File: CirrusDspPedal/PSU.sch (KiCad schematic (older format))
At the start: 5 parts, among them J4 Barrel_Jack_Switch, U5 MCP1700-3302E_SOT23

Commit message: Added Footswitches and relay
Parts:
- D1: footprint (none) -> Diode_SMD:D_SOD-123F
- J4: footprint (none) -> Connector_BarrelJack:BarrelJack_Horizontal
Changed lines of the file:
@@
 $Descr A4 11693 8268
 encoding utf-8
-Sheet 8 8
+Sheet 8 10
 Title ""
 Date ""
@@
 F 0 "D1" H 4800 3358 50  0000 C CNN
 F 1 "D_Schottky" H 4800 3449 50  0000 C CNN
-F 2 "" H 4800 3575 50  0001 C CNN
+F 2 "Diode_SMD:D_SOD-123F" H 4800 3575 50  0001 C CNN
 F 3 "~" H 4800 3575 50  0001 C CNN
 	1    4800 3575
@@
 F 0 "J4" H 2950 3375 50  0000 R CNN
 F 1 "Barrel_Jack_Switch" H 3575 3450 50  0000 R CNN
-F 2 "" H 3125 3635 50  0001 C CNN
+F 2 "Connector_BarrelJack:BarrelJack_Horizontal" H 3125 3635 50  0001 C CNN
 F 3 "~" H 3125 3635 50  0001 C CNN
 	1    3075 3675

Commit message: Completed schematic design
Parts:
- added J7: Conn_01x01, TestPoint:TestPoint_Pad_2.0x2.0mm, symbol Connector_Generic:Conn_01x01
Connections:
- new net GNDPWR: J7.1 (Pin_1)
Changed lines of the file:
@@
 $Descr A4 11693 8268
 encoding utf-8
-Sheet 8 10
+Sheet 6 11
 Title ""
 Date ""
@@
 Wire Wire Line
 	7525 3575 8700 3575
+$Comp
+L power:GNDPWR #PWR016
+U 1 1 5FB2677B
+P 5575 5950
+F 0 "#PWR016" H 5575 5750 50  0001 C CNN
+F 1 "GNDPWR" H 5579 5796 50  0000 C CNN
+F 2 "" H 5575 5900 50  0001 C CNN
+F 3 "" H 5575 5900 50  0001 C CNN
+	1    5575 5950
+	1    0    0    -1
+$EndComp
+Wire Wire Line
+	5575 5950 5575 5825
+$Comp
+L Connector_Generic:Conn_01x01 J7
+U 1 1 5FB27261
+P 5575 5525
+F 0 "J7" V 5493 5437 50  0000 R CNN
+F 1 "Conn_01x01" V 5448 5437 50  0001 R CNN
+F 2 "TestPoint:TestPoint_Pad_2.0x2.0mm" H 5575 5525 50  0001 C CNN
+F 3 "~" H 5575 5525 50  0001 C CNN
+	1    5575 5525
+	0    -1   -1   0
+$EndComp
+$Comp
+L power:PWR_FLAG #FLG0106
+U 1 1 5FB29381
+P 5775 5825
+F 0 "#FLG0106" H 5775 5900 50  0001 C CNN
+F 1 "PWR_FLAG" H 5775 5998 50  0001 C CNN
+F 2 "" H 5775 5825 50  0001 C CNN
+F 3 "~" H 5775 5825 50  0001 C CNN
+	1    5775 5825
+	0    1    1    0
+$EndComp
+Wire Wire Line
+	5775 5825 5575 5825
+Connection ~ 5575 5825
+Wire Wire Line
+	5575 5825 5575 5725
 $EndSCHEMATC

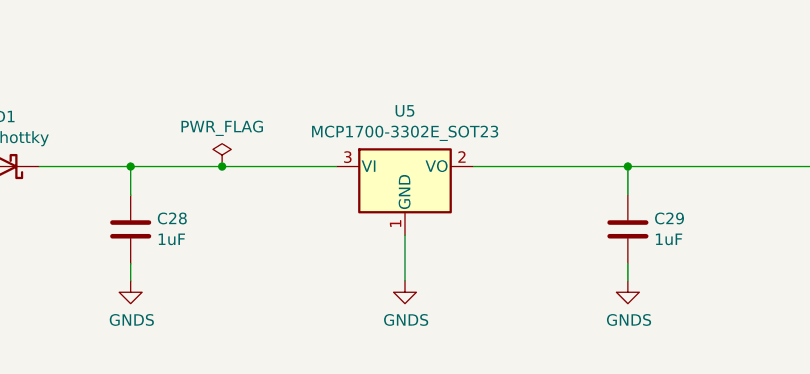
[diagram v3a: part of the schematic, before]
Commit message: updated design and layout
- Changed LDO to 1703 (footprint unchanged)
- Changed THT LEDs from RAGB (incorrect) to RCGB (correct) symbol (footprint unchanged)
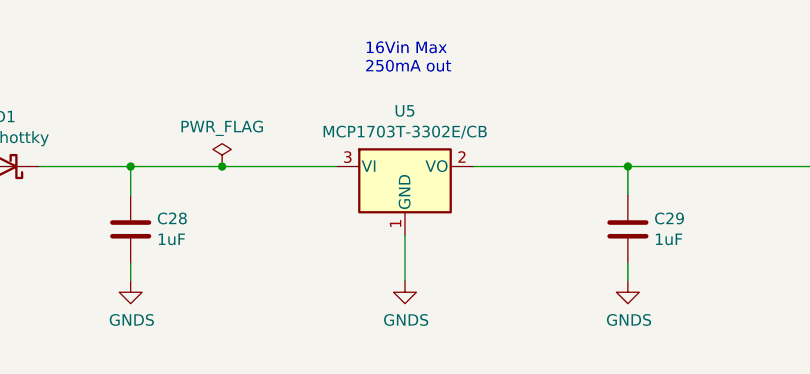
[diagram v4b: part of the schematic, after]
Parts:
- U5: value MCP1700-3302E_SOT23 -> MCP1703T-3302E/CB
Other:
- note added: "16Vin Max\n250mA out"
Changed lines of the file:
@@
 P 6550 3575
 F 0 "U5" H 6550 3817 50  0000 C CNN
-F 1 "MCP1700-3302E_SOT23" H 6550 3726 50  0000 C CNN
+F 1 "MCP1703T-3302E/CB" H 6550 3726 50  0000 C CNN
 F 2 "Package_TO_SOT_SMD:SOT-23" H 6550 3800 50  0001 C CNN
-F 3 "http://ww1.microchip.com/downloads/en/DeviceDoc/20001826D.pdf" H 6550 3575 50  0001 C CNN
+F 3 "https://ww1.microchip.com/downloads/en/DeviceDoc/22049f.pdf" H 6550 3575 50  0001 C CNN
 	1    6550 3575
 	1    0    0    -1
@@
 Wire Wire Line
 	5575 5825 5575 5725
+Text Notes 6375 3175 0    50   ~ 0
+16Vin Max\n250mA out
 $EndSCHEMATC

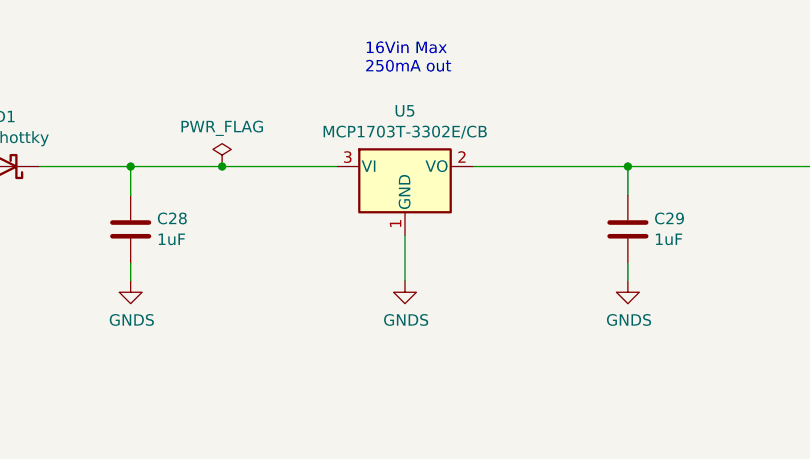
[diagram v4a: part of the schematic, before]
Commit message: updated design and layout
- Changed LDO package from SOT23 to SOT223
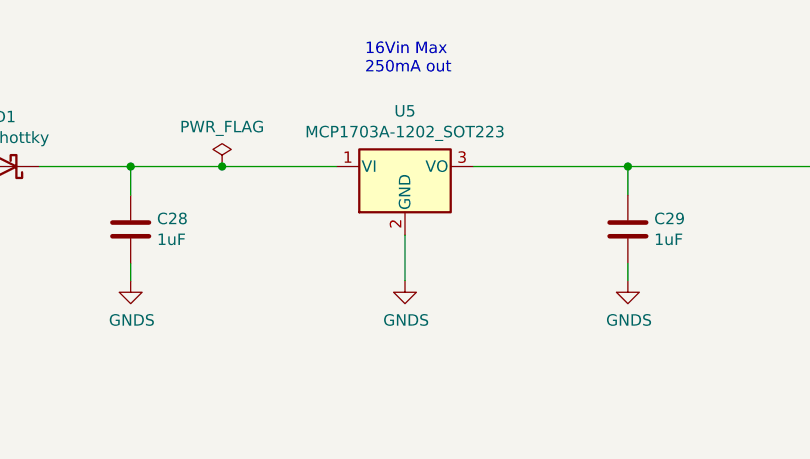
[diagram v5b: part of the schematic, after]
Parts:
- removed U5: MCP1703T-3302E/CB, Package_TO_SOT_SMD:SOT-23, symbol Regulator_Linear:MCP1700-3302E_SOT23
- added U5: MCP1703A-1202_SOT223, Package_TO_SOT_SMD:SOT-223-3_TabPin2, symbol Regulator_Linear:MCP1703A-1202_SOT223
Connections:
- net +3V3: now also U5.3 (VO)
- net GNDS: now also U5.2 (GND)
- net at C28.1, D1.1 (K): now also U5.1 (VI)
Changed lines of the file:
@@
 $EndDescr
-$Comp
-L Regulator_Linear:MCP1700-3302E_SOT23 U5
-U 1 1 5F95E7A8
-P 6550 3575
-F 0 "U5" H 6550 3817 50  0000 C CNN
-F 1 "MCP1703T-3302E/CB" H 6550 3726 50  0000 C CNN
-F 2 "Package_TO_SOT_SMD:SOT-23" H 6550 3800 50  0001 C CNN
-F 3 "https://ww1.microchip.com/downloads/en/DeviceDoc/22049f.pdf" H 6550 3575 50  0001 C CNN
-	1    6550 3575
-	1    0    0    -1
-$EndComp
 $Comp
 L Device:D_Schottky D1
@@
 Text Notes 6375 3175 0    50   ~ 0
 16Vin Max\n250mA out
+$Comp
+L Regulator_Linear:MCP1703A-1202_SOT223 U5
+U 1 1 5F9DD190
+P 6550 3575
+F 0 "U5" H 6550 3817 50  0000 C CNN
+F 1 "MCP1703A-1202_SOT223" H 6550 3726 50  0000 C CNN
+F 2 "Package_TO_SOT_SMD:SOT-223-3_TabPin2" H 6550 3775 50  0001 C CNN
+F 3 "http://ww1.microchip.com/downloads/en/DeviceDoc/20005122B.pdf" H 6550 3525 50  0001 C CNN
+	1    6550 3575
+	1    0    0    -1
+$EndComp
 $EndSCHEMATC

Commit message: finished revb layout
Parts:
- added C23, C24: 1uF, Capacitor_SMD:C_1206_3216Metric_Pad1.42x1.75mm_HandSolder, symbol Device:C
- added U4: SE8250X2_SOT23, Package_TO_SOT_SMD:SOT-23, symbol Regulator_Linear:MCP1700-5002E_SOT23
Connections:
- net GNDS: now also C23.2, C24.2, U4.1 (GND)
- net at C28.1, D1.1 (K), U5.1 (VI): now also C23.1, U4.3 (VI)
- new net +5V: C24.1, U4.2 (VO)
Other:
- note added: "30Vin Max\n100mA out"
- moved on the sheet: C28, C29, D1, J4, J7, U5

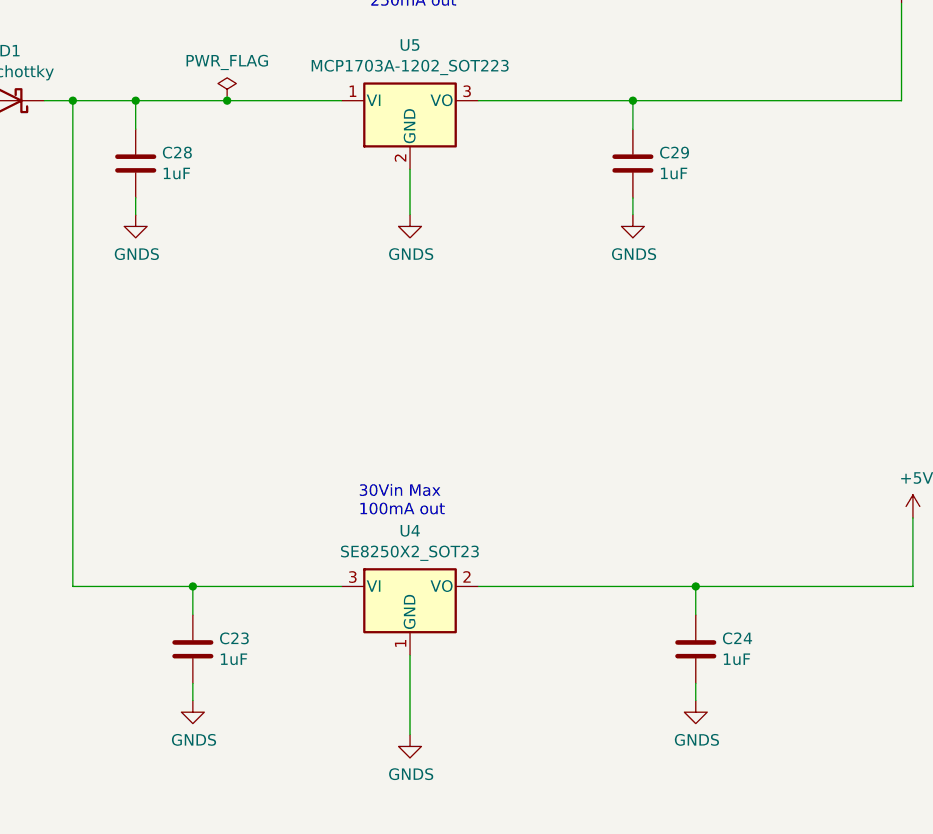
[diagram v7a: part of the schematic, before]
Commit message: updated revB
- Added higher out current LDO (LD1117) for 5V rail
- Added jumper on OLED connector to select 3V3/5V
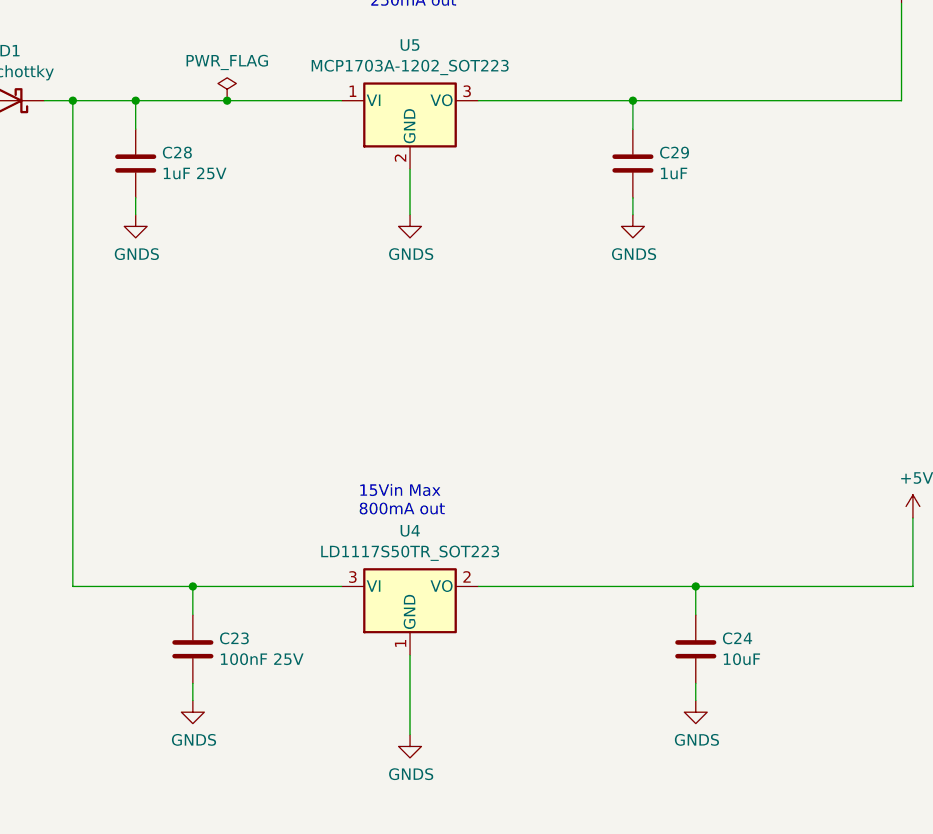
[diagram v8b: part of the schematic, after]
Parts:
- removed U4: SE8250X2_SOT23, Package_TO_SOT_SMD:SOT-23, symbol Regulator_Linear:MCP1700-5002E_SOT23
- added U4: LD1117S50TR_SOT223, Package_TO_SOT_SMD:SOT-223-3_TabPin2, symbol Regulator_Linear:LD1117S50TR_SOT223
- C23: value 1uF -> 100nF 25V
- C24: value 1uF -> 10uF
- C28: value 1uF -> 1uF 25V
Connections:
- net +5V: now also U4.2 (VO)
- net GNDS: now also U4.1 (GND)
- net at C23.1, C28.1, D1.1 (K)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: now also U4.3 (VI)
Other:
- note added: "15Vin Max\n800mA out"
- note removed: "30Vin Max\n100mA out"
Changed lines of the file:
@@
 P 5000 2725
 F 0 "C28" H 5115 2771 50  0000 L CNN
-F 1 "1uF" H 5115 2680 50  0000 L CNN
+F 1 "1uF 25V" H 5115 2680 50  0000 L CNN
 F 2 "Capacitor_SMD:C_1206_3216Metric_Pad1.42x1.75mm_HandSolder" H 5038 2575 50  0001 C CNN
 F 3 "~" H 5000 2725 50  0001 C CNN
@@
 	1    0    0    -1
 $EndComp
-$Comp
-L Regulator_Linear:MCP1700-5002E_SOT23 U4
-U 1 1 5FA5721B
-P 6200 4575
-F 0 "U4" H 6200 4817 50  0000 C CNN
-F 1 "SE8250X2_SOT23" H 6200 4726 50  0000 C CNN
-F 2 "Package_TO_SOT_SMD:SOT-23" H 6200 4800 50  0001 C CNN
-F 3 "https://datasheet.lcsc.com/szlcsc/1912111437_Seaward-Elec-SE8250X2_C437589.pdf" H 6200 4575 50  0001 C CNN
-	1    6200 4575
-	1    0    0    -1
-$EndComp
 Wire Wire Line
 	5900 4575 5250 4575
@@
 P 5250 4850
 F 0 "C23" H 5365 4896 50  0000 L CNN
-F 1 "1uF" H 5365 4805 50  0000 L CNN
+F 1 "100nF 25V" H 5365 4805 50  0000 L CNN
 F 2 "Capacitor_SMD:C_1206_3216Metric_Pad1.42x1.75mm_HandSolder" H 5288 4700 50  0001 C CNN
 F 3 "~" H 5250 4850 50  0001 C CNN
@@
 P 7450 4850
 F 0 "C24" H 7565 4896 50  0000 L CNN
-F 1 "1uF" H 7565 4805 50  0000 L CNN
+F 1 "10uF" H 7565 4805 50  0000 L CNN
 F 2 "Capacitor_SMD:C_1206_3216Metric_Pad1.42x1.75mm_HandSolder" H 7488 4700 50  0001 C CNN
 F 3 "~" H 7450 4850 50  0001 C CNN
@@
 	7450 4575 8400 4575
 Text Notes 5975 4275 0    50   ~ 0
-30Vin Max\n100mA out
+15Vin Max\n800mA out
+$Comp
+L Regulator_Linear:LD1117S50TR_SOT223 U4
+U 1 1 5FAACAF4
+P 6200 4575
+F 0 "U4" H 6200 4817 50  0000 C CNN
+F 1 "LD1117S50TR_SOT223" H 6200 4726 50  0000 C CNN
+F 2 "Package_TO_SOT_SMD:SOT-223-3_TabPin2" H 6200 4775 50  0001 C CNN
+F 3 "http://www.st.com/st-web-ui/static/active/en/resource/technical/document/datasheet/CD00000544.pdf" H 6300 4325 50  0001 C CNN
+	1    6200 4575
+	1    0    0    -1
+$EndComp
 $EndSCHEMATC
